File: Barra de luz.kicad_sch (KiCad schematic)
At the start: 7 parts, among them J3 AVR-ISP-6, SW1 SW_Push, U1 ATtiny85-20S

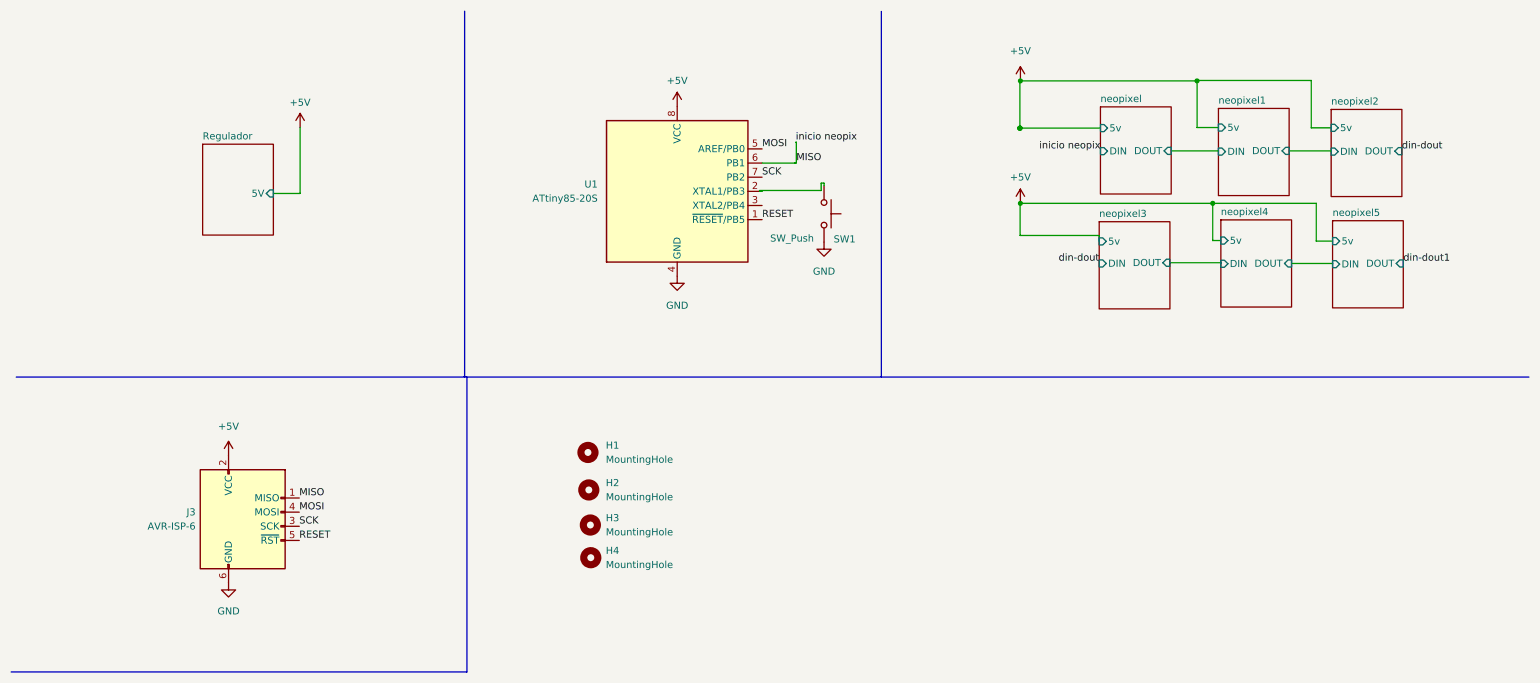
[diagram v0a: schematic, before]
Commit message: ajustes para quitar leds y hacer placa mas sencilla
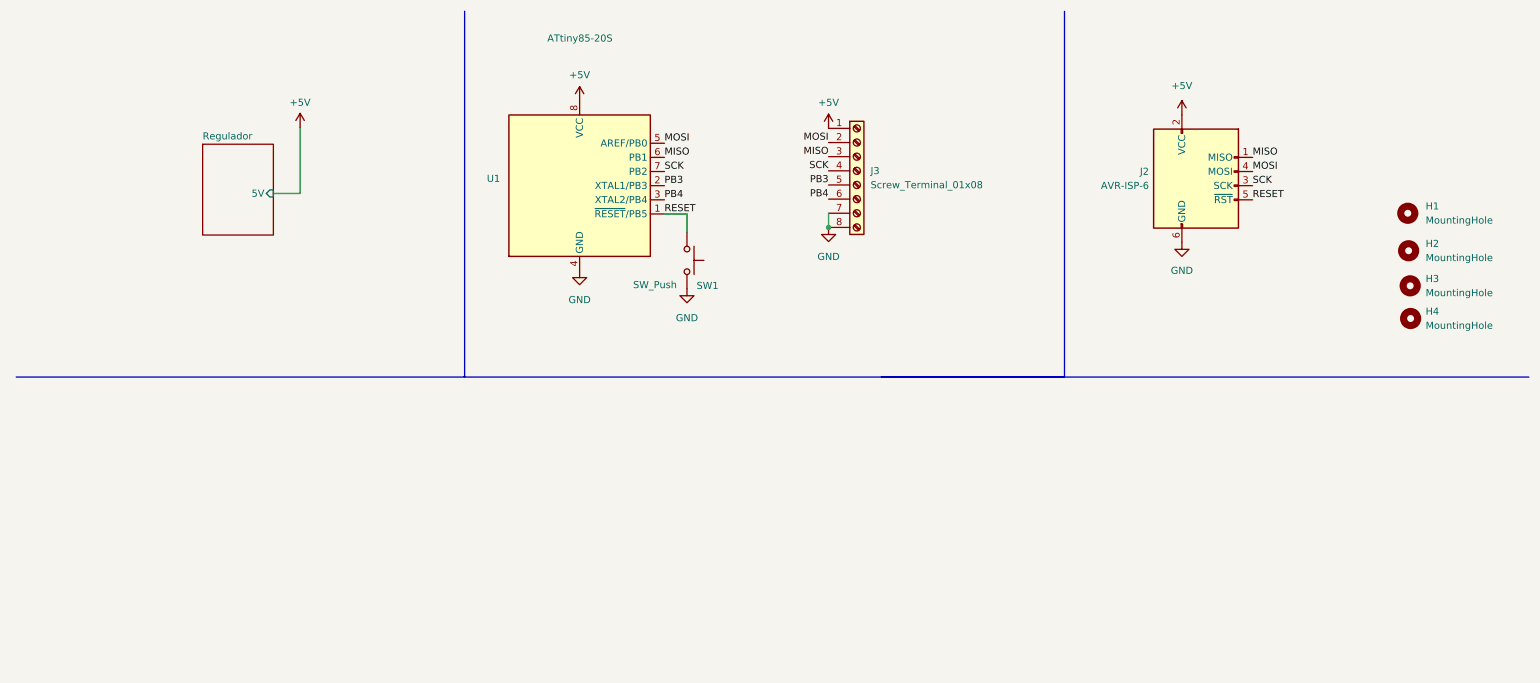
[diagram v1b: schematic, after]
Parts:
- removed J3: AVR-ISP-6, Connector_PinSocket_2.54mm:PinSocket_2x03_P2.54mm_Vertical, symbol Connector:AVR-ISP-6
- added J2: AVR-ISP-6, Connector_PinSocket_2.54mm:PinSocket_2x03_P2.54mm_Vertical, symbol Connector:AVR-ISP-6
- added J3: Screw_Terminal_01x08, TerminalBlock_Phoenix:TerminalBlock_Phoenix_MKDS-3-8-5.08_1x08_P5.08mm_Horizontal, symbol Connector:Screw_Terminal_01x08
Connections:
- net +5V: now also J2.2 (VCC), J3.1 (Pin_1)
- net GND: now also J2.6 (GND), J3.7 (Pin_7), J3.8 (Pin_8)
- net MISO: now also J2.1 (MISO), J3.3 (Pin_3)
- net MOSI: now also J2.4 (MOSI), J3.2 (Pin_2)
- net RESET: now also SW1.1, J2.5 (~{RST})
- net SCK: now also J2.3 (SCK), J3.4 (Pin_4)
- net PB3: now reaches U1.2 (XTAL1/PB3)
- net PB3: now also J3.5 (Pin_5); no longer SW1.1
- net PB4: now reaches U1.3 (XTAL2/PB4)
- net PB4: now also J3.6 (Pin_6)
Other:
- removed sheet neopixel
- removed sheet neopixel1
- removed sheet neopixel2
- removed sheet neopixel3
- removed sheet neopixel4
- removed sheet neopixel5
- moved on the sheet: H1, H2, H3, H4, SW1, U1
